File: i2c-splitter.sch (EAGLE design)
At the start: 4 parts

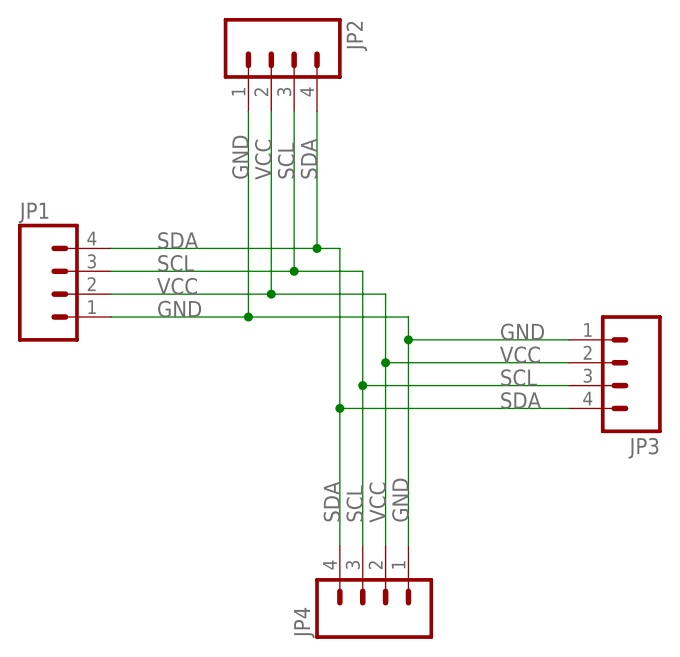
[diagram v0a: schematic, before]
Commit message: optional bypass capacitor
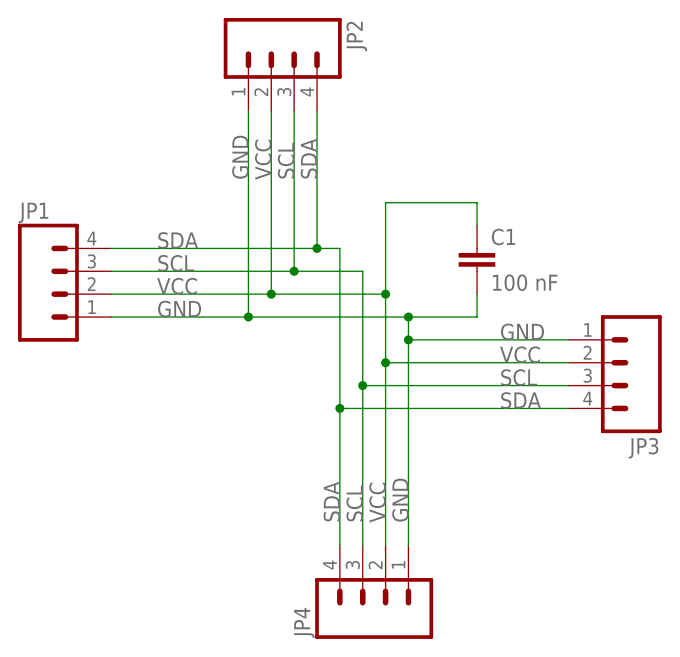
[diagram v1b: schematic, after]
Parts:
- added C1: 100 nF, resistor:C-EUC0805
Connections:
- net GND: now also C1.2
- net VCC: now also C1.1
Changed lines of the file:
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@@
 <part name="JP3" library="SparkFun" deviceset="M04" device="PTH"/>
 <part name="JP4" library="SparkFun" deviceset="M04" device="PTH"/>
+<part name="C1" library="resistor" deviceset="C-EU" device="C0805" value="100 nF"/>
 </parts>
 <sheets>
@@
 <instance part="JP3" gate="G$1" x="33.02" y="63.5" rot="R180"/>
 <instance part="JP4" gate="G$1" x="7.62" y="38.1" rot="R90"/>
+<instance part="C1" gate="G$1" x="17.78" y="76.2"/>
 </instances>
 <busses>
@@
 <label x="-7.62" y="83.82" size="1.778" layer="95" rot="R90"/>
 <label x="10.16" y="45.72" size="1.778" layer="95" rot="R90"/>
+<junction x="10.16" y="68.58"/>
+<pinref part="C1" gate="G$1" pin="2"/>
+<wire x1="10.16" y1="68.58" x2="17.78" y2="68.58" width="0.1524" layer="91"/>
+<wire x1="17.78" y1="68.58" x2="17.78" y2="71.12" width="0.1524" layer="91"/>
 </segment>
 </net>
@@
 <label x="-5.08" y="83.82" size="1.778" layer="95" rot="R90"/>
 <label x="7.62" y="45.72" size="1.778" layer="95" rot="R90"/>
+<junction x="7.62" y="71.12"/>
+<pinref part="C1" gate="G$1" pin="1"/>
+<wire x1="17.78" y1="78.74" x2="17.78" y2="81.28" width="0.1524" layer="91"/>
+<wire x1="17.78" y1="81.28" x2="7.62" y2="81.28" width="0.1524" layer="91"/>
+<wire x1="7.62" y1="81.28" x2="7.62" y2="71.12" width="0.1524" layer="91"/>
 </segment>
 </net>
